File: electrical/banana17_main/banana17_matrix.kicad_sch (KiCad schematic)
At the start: 36 parts, among them SW1 SW, SW10 SW, SW11 SW, SW12 SW, SW13 SW, SW14 SW, SW15 SW, SW17 SW, SW18 SW, SW19 SW, SW2 SW, SW21 RotaryEncoder_Switch, SW3 SW, SW4 SW, SW6 SW, SW7 SW, SW8 SW, SW9 SW

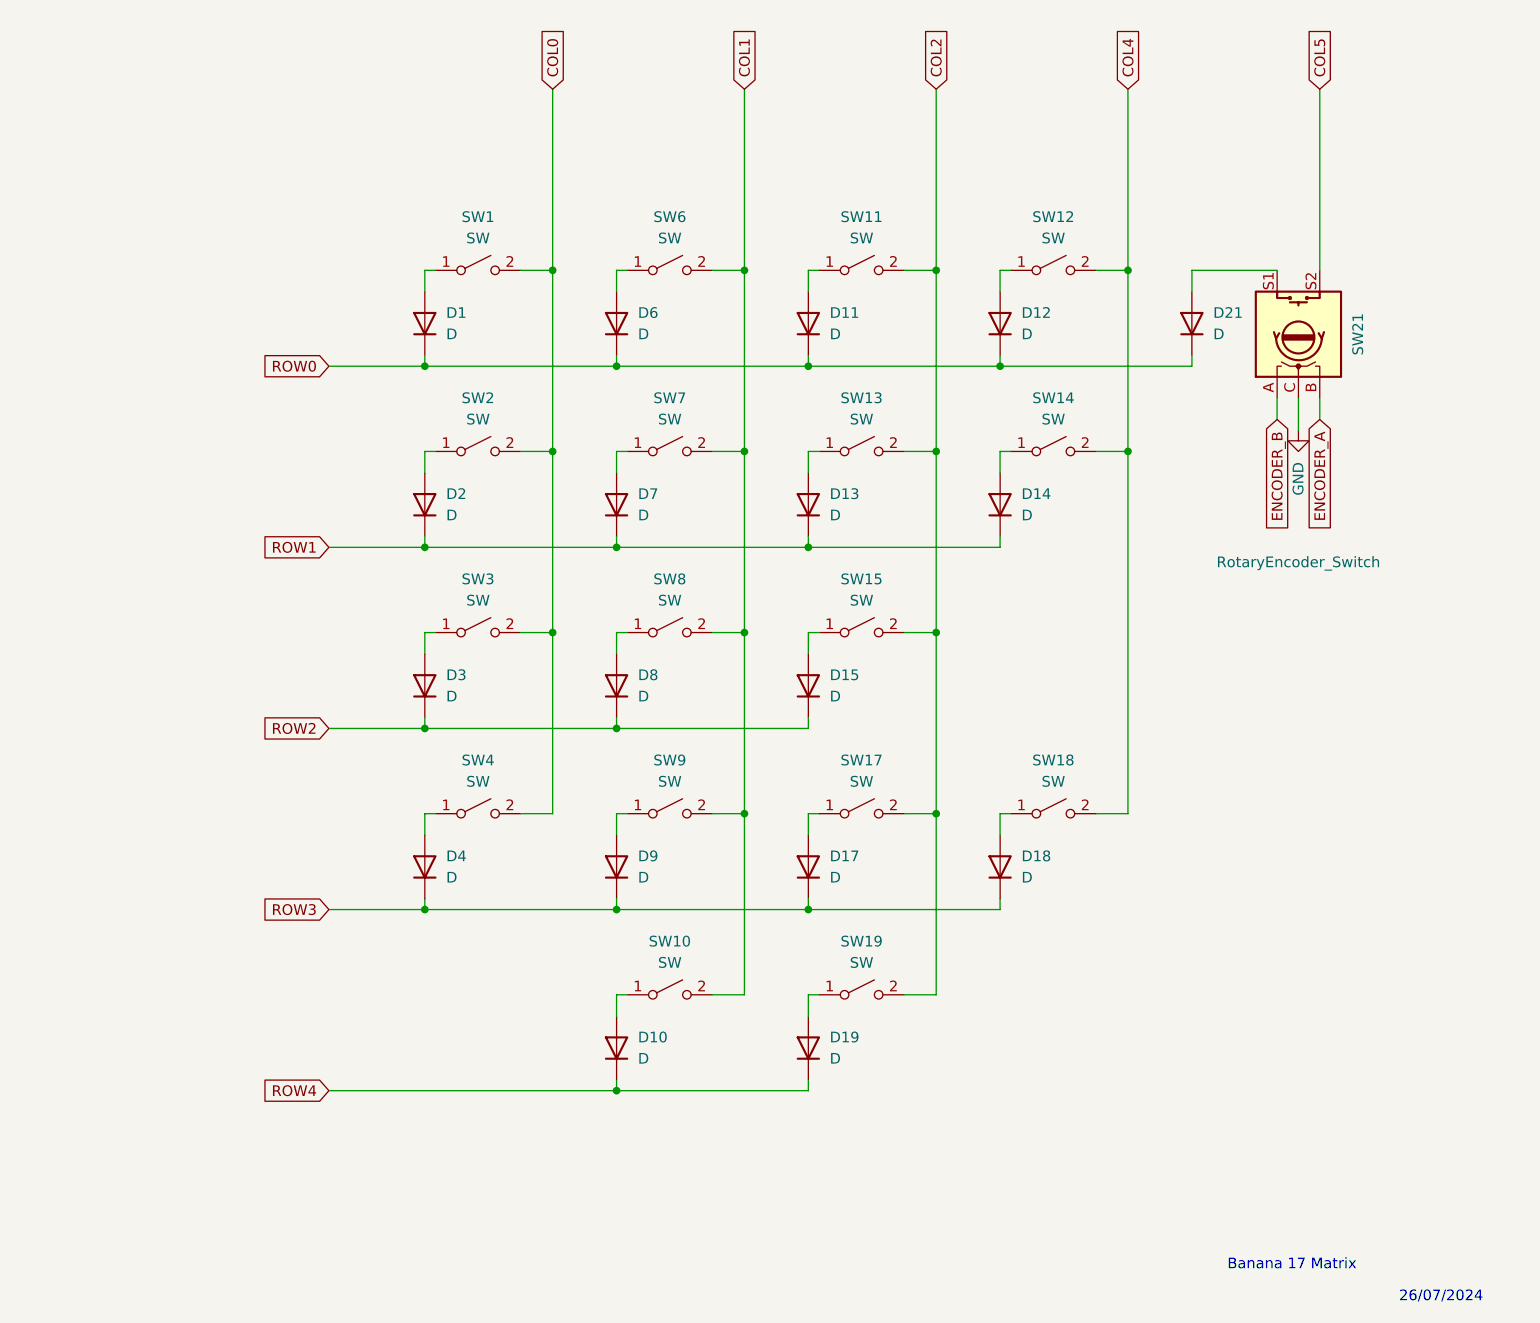
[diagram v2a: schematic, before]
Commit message: Uploaded library for SSD1306 128x32.
Uploaded library for SSD1306 128x32. This needs to be tested first prior to usage.
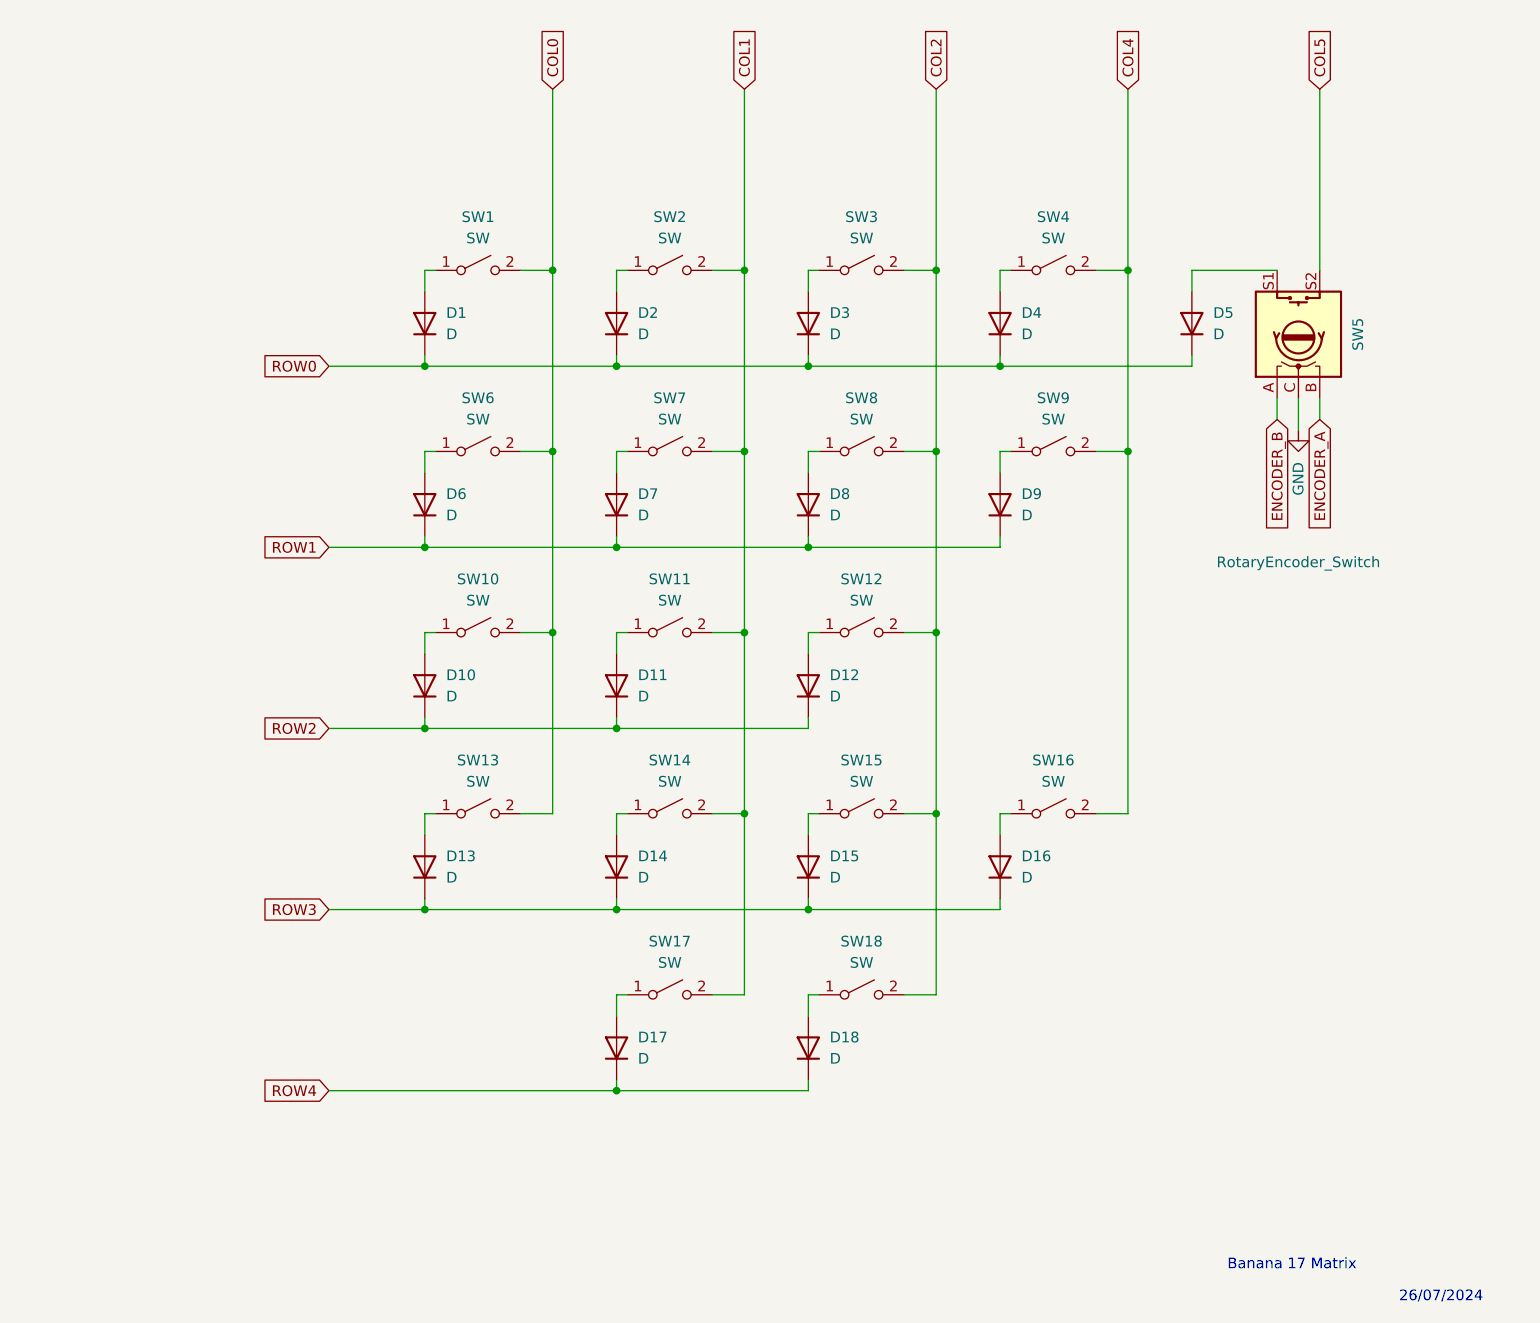
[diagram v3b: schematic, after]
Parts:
- renumbered D3 to D10, D8 to D11, D15 to D12, D4 to D13, D9 to D14, D17 to D15, D18 to D16, D10 to D17, D19 to D18, D6 to D2, D11 to D3, D12 to D4, D21 to D5, D2 to D6, D13 to D8, D14 to D9, SW3 to SW10, SW8 to SW11, SW15 to SW12, SW4 to SW13, SW9 to SW14, SW17 to SW15, SW18 to SW16, SW10 to SW17, SW19 to SW18, SW6 to SW2, SW11 to SW3, SW12 to SW4, SW21 to SW5, SW2 to SW6, SW13 to SW8, SW14 to SW9

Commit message: Initial footprint all selected. Schematic capture complete.
Initial footprint all selected. Schematic capture complete.
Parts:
- D1, D10, D11, D12, D13, D14, D15, D16, D17, D18, D2, D3, D4, D5, D6, D7, D8, D9: footprint (none) -> Diode_SMD:D_0805_2012Metric_Pad1.15x1.40mm_HandSolder
- SW1, SW10, SW11, SW12, SW13, SW14, SW15, SW18, SW2, SW3, SW4, SW6, SW7, SW8: footprint (none) -> Button_Switch_Keyboard:SW_Cherry_MX_1.00u_PCB
- SW16, SW9: footprint (none) -> Button_Switch_Keyboard:SW_Cherry_MX_2.00u_Vertical_PCB
- SW17: footprint (none) -> Button_Switch_Keyboard:SW_Cherry_MX_2.00u_PCB
- SW5: footprint (none) -> Rotary_Encoder:RotaryEncoder_Alps_EC11E-Switch_Vertical_H20mm
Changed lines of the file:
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@@
 			)
 		)
-		(property "Footprint" ""
+		(property "Footprint" "Diode_SMD:D_0805_2012Metric_Pad1.15x1.40mm_HandSolder"
 			(at 137.16 142.24 0)
 			(effects
@@
 			)
 		)
-		(property "Footprint" ""
+		(property "Footprint" "Diode_SMD:D_0805_2012Metric_Pad1.15x1.40mm_HandSolder"
 			(at 91.44 142.24 0)
 			(effects
@@
 			)
 		)
-		(property "Footprint" ""
+		(property "Footprint" "Diode_SMD:D_0805_2012Metric_Pad1.15x1.40mm_HandSolder"
 			(at 137.16 77.47 0)
 			(effects
@@
 			)
 		)
-		(property "Footprint" ""
+		(property "Footprint" "Diode_SMD:D_0805_2012Metric_Pad1.15x1.40mm_HandSolder"
 			(at 114.3 120.65 0)
 			(effects
@@
 			)
 		)
-		(property "Footprint" ""
+		(property "Footprint" "Diode_SMD:D_0805_2012Metric_Pad1.15x1.40mm_HandSolder"
 			(at 160.02 99.06 0)
 			(effects
@@
 			)
 		)
-		(property "Footprint" ""
+		(property "Footprint" "Button_Switch_Keyboard:SW_Cherry_MX_2.00u_Vertical_PCB"
 			(at 166.37 135.89 0)
 			(effects
@@
 			)
 		)
-		(property "Footprint" ""
+		(property "Footprint" "Button_Switch_Keyboard:SW_Cherry_MX_2.00u_PCB"
 			(at 120.65 157.48 0)
 			(effects
@@
 			)
 		)
-		(property "Footprint" ""
+		(property "Footprint" "Diode_SMD:D_0805_2012Metric_Pad1.15x1.40mm_HandSolder"
 			(at 91.44 120.65 0)
 			(effects
@@
 			)
 		)
-		(property "Footprint" ""
+		(property "Footprint" "Diode_SMD:D_0805_2012Metric_Pad1.15x1.40mm_HandSolder"
 			(at 182.88 77.47 0)
 			(effects
@@
 			)
 		)
-		(property "Footprint" ""
+		(property "Footprint" "Button_Switch_Keyboard:SW_Cherry_MX_1.00u_PCB"
 			(at 97.79 135.89 0)
 			(effects
@@
 			)
 		)
-		(property "Footprint" ""
+		(property "Footprint" "Button_Switch_Keyboard:SW_Cherry_MX_1.00u_PCB"
 			(at 143.51 114.3 0)
 			(effects
@@
 			)
 		)
-		(property "Footprint" ""
+		(property "Footprint" "Button_Switch_Keyboard:SW_Cherry_MX_1.00u_PCB"
 			(at 143.51 157.48 0)
 			(effects
@@
 			)
 		)
-		(property "Footprint" ""
+		(property "Footprint" "Button_Switch_Keyboard:SW_Cherry_MX_1.00u_PCB"
 			(at 120.65 71.12 0)
 			(effects
@@
 			)
 		)
-		(property "Footprint" ""
+		(property "Footprint" "Button_Switch_Keyboard:SW_Cherry_MX_1.00u_PCB"
 			(at 97.79 92.71 0)
 			(effects
@@
 			)
 		)
-		(property "Footprint" ""
+		(property "Footprint" "Diode_SMD:D_0805_2012Metric_Pad1.15x1.40mm_HandSolder"
 			(at 114.3 77.47 0)
 			(effects
@@
 			)
 		)
-		(property "Footprint" ""
+		(property "Footprint" "Button_Switch_Keyboard:SW_Cherry_MX_1.00u_PCB"
 			(at 166.37 71.12 0)
 			(effects
@@
 			)
 		)
-		(property "Footprint" ""
+		(property "Footprint" "Button_Switch_Keyboard:SW_Cherry_MX_1.00u_PCB"
 			(at 120.65 114.3 0)
 			(effects
@@
 			)
 		)
-		(property "Footprint" ""
+		(property "Footprint" "Button_Switch_Keyboard:SW_Cherry_MX_1.00u_PCB"
 			(at 143.51 71.12 0)
 			(effects
@@
 			)
 		)
-		(property "Footprint" ""
+		(property "Footprint" "Button_Switch_Keyboard:SW_Cherry_MX_1.00u_PCB"
 			(at 120.65 135.89 0)
 			(effects
@@
 			)
 		)
-		(property "Footprint" ""
+		(property "Footprint" "Button_Switch_Keyboard:SW_Cherry_MX_1.00u_PCB"
 			(at 143.51 92.71 0)
 			(effects
@@
 			)
 		)
-		(property "Footprint" ""
+		(property "Footprint" "Diode_SMD:D_0805_2012Metric_Pad1.15x1.40mm_HandSolder"
 			(at 114.3 99.06 0)
 			(effects
@@
 			)
 		)
-		(property "Footprint" ""
+		(property "Footprint" "Diode_SMD:D_0805_2012Metric_Pad1.15x1.40mm_HandSolder"
 			(at 160.02 142.24 0)
 			(effects
@@
 			)
 		)
-		(property "Footprint" ""
+		(property "Footprint" "Diode_SMD:D_0805_2012Metric_Pad1.15x1.40mm_HandSolder"
 			(at 137.16 163.83 0)
 			(effects
@@
 			)
 		)
-		(property "Footprint" ""
+		(property "Footprint" "Button_Switch_Keyboard:SW_Cherry_MX_1.00u_PCB"
 			(at 120.65 92.71 0)
 			(effects
@@
 			)
 		)
-		(property "Footprint" ""
+		(property "Footprint" "Diode_SMD:D_0805_2012Metric_Pad1.15x1.40mm_HandSolder"
 			(at 137.16 99.06 0)
 			(effects
@@
 			)
 		)
-		(property "Footprint" ""
+		(property "Footprint" "Button_Switch_Keyboard:SW_Cherry_MX_1.00u_PCB"
 			(at 97.79 71.12 0)
 			(effects
@@
 			)
 		)
-		(property "Footprint" ""
+		(property "Footprint" "Diode_SMD:D_0805_2012Metric_Pad1.15x1.40mm_HandSolder"
 			(at 91.44 99.06 0)
 			(effects
@@
 			)
 		)
-		(property "Footprint" ""
+		(property "Footprint" "Diode_SMD:D_0805_2012Metric_Pad1.15x1.40mm_HandSolder"
 			(at 114.3 163.83 0)
 			(effects
@@
 			)
 		)
-		(property "Footprint" ""
+		(property "Footprint" "Diode_SMD:D_0805_2012Metric_Pad1.15x1.40mm_HandSolder"
 			(at 114.3 142.24 0)
 			(effects
@@
 			)
 		)
-		(property "Footprint" ""
+		(property "Footprint" "Diode_SMD:D_0805_2012Metric_Pad1.15x1.40mm_HandSolder"
 			(at 91.44 77.47 0)
 			(effects
@@
 			)
 		)
-		(property "Footprint" ""
+		(property "Footprint" "Rotary_Encoder:RotaryEncoder_Alps_EC11E-Switch_Vertical_H20mm"
 			(at 191.516 82.55 0)
 			(effects
@@
 			)
 		)
-		(property "Footprint" ""
+		(property "Footprint" "Button_Switch_Keyboard:SW_Cherry_MX_1.00u_PCB"
 			(at 97.79 114.3 0)
 			(effects
@@
 			)
 		)
-		(property "Footprint" ""
+		(property "Footprint" "Button_Switch_Keyboard:SW_Cherry_MX_1.00u_PCB"
 			(at 143.51 135.89 0)
 			(effects
@@
 			)
 		)
-		(property "Footprint" ""
+		(property "Footprint" "Diode_SMD:D_0805_2012Metric_Pad1.15x1.40mm_HandSolder"
 			(at 160.02 77.47 0)
 			(effects
@@
 			)
 		)
-		(property "Footprint" ""
+		(property "Footprint" "Button_Switch_Keyboard:SW_Cherry_MX_2.00u_Vertical_PCB"
 			(at 166.37 92.71 0)
 			(effects
@@
 			)
 		)
-		(property "Footprint" ""
+		(property "Footprint" "Diode_SMD:D_0805_2012Metric_Pad1.15x1.40mm_HandSolder"
 			(at 137.16 120.65 0)
 			(effects
